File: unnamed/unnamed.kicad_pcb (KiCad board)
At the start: 2 copper layers, 33 parts, among them SW1 SW_Push, SW10 SW_Push, SW11 SW_Push, SW12 SW_Push, SW13 SW_Push, SW14 SW_Push, SW15 SW_Push, SW16 SW_Push, SW17 SW_Push, SW18 SW_Push, SW19 SW_Push, SW2 SW_Push, SW20 SW_Push, SW21 SW_Push, SW22 SW_Push, SW23 SW_Push, SW24 SW_Push, SW25 SW_SPST, SW26 SW_SPST, SW27 SW_Push, SW28 SW_Push, SW29 SW_Push, SW3 SW_Push, SW30 SW_Push, SW31 SW_Push, SW32 SW_Push, SW33 SW_Push, SW4 SW_Push, SW5 SW_Push, SW6 SW_Push, SW7 SW_Push, SW8 SW_Push, SW9 SW_Push

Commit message: place switches
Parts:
- moved SW17 212.8 mm to (201.4, 106.7), turned to -30 degrees
- moved SW16 175.6 mm to (181.7, 98.4), turned to -15 degrees
- moved SW1 116.6 mm to (115.4, 51.2)
- moved SW2 115.9 mm to (115.4, 70.2)
- moved SW9 115.8 mm to (153.4, 71.1)
- moved SW3 115.8 mm to (115.4, 89.2)
- moved SW8 115.7 mm to (153.4, 52.1)
- moved SW13 115.5 mm to (191.4, 40.2)
- moved SW12 115.5 mm to (172.4, 75.7)
- moved SW4 115.5 mm to (134.4, 39.2)
- moved SW7 115.5 mm to (153.4, 33.1)
- moved SW6 115.5 mm to (134.4, 77.2)
- moved SW11 115.5 mm to (172.4, 56.6)
- moved SW10 115.5 mm to (172.4, 37.6)
- moved SW15 115.4 mm to (191.4, 78.2)
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
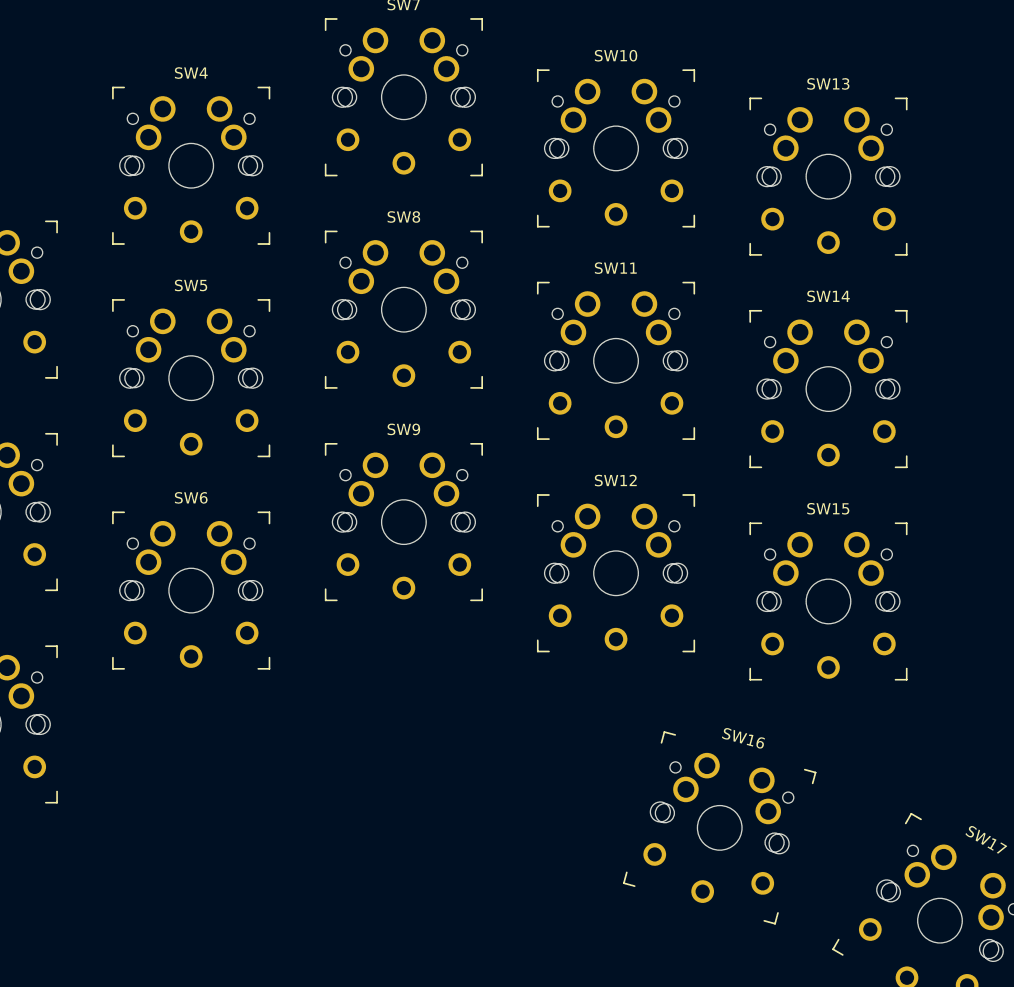
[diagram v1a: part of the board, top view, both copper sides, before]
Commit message: component placement
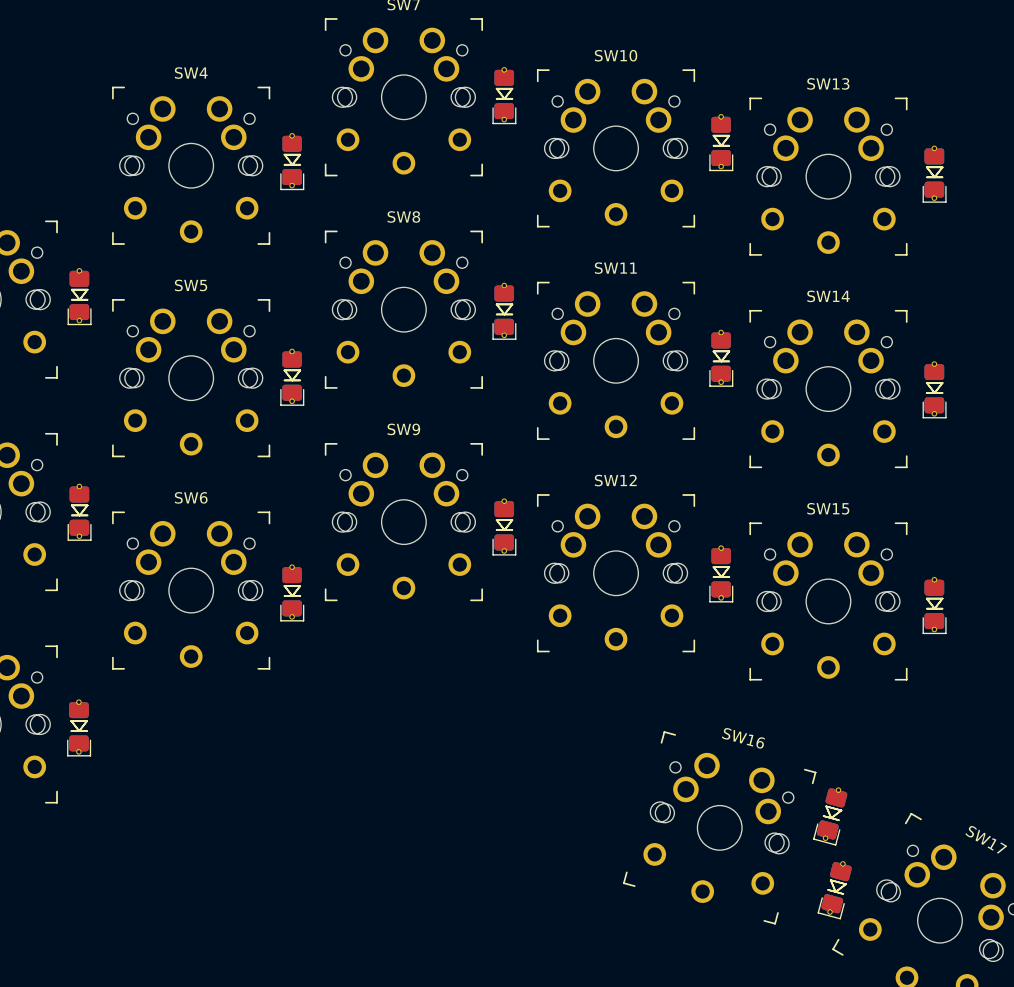
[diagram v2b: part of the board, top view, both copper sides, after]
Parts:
- added D10: D, Library:D_1206_handsolder_reversible, F.Cu at (143.4, 77.3)
- added D13: D, Library:D_1206_handsolder_reversible, F.Cu at (162.4, 32.8)
- added D14: D, Library:D_1206_handsolder_reversible, F.Cu at (162.4, 52.1)
- added D15: D, Library:D_1206_handsolder_reversible, F.Cu at (162.4, 71.4)
- added D18: D, Library:D_1206_handsolder_reversible, F.Cu at (181.8, 37.0)
- added D19: D, Library:D_1206_handsolder_reversible, F.Cu at (181.8, 56.3)
- added D20: D, Library:D_1206_handsolder_reversible, F.Cu at (181.8, 75.6)
- added D24: D, Library:D_1206_handsolder_reversible, F.Cu at (200.9, 39.9)
- added D25: D, Library:D_1206_handsolder_reversible, F.Cu at (200.9, 59.1)
- added D26: D, Library:D_1206_handsolder_reversible, F.Cu at (200.9, 78.4)
- added D3: D, Library:D_1206_handsolder_reversible, F.Cu at (124.4, 50.8)
- added D30: D, Library:D_1206_handsolder_reversible, F.Cu at (191.8, 97.2)
- added D33: D, Library:D_1206_handsolder_reversible, F.Cu at (192.2, 103.8)
- added D4: D, Library:D_1206_handsolder_reversible, F.Cu at (124.4, 70.1)
- added D5: D, Library:D_1206_handsolder_reversible, F.Cu at (124.4, 89.4)
- added D8: D, Library:D_1206_handsolder_reversible, F.Cu at (143.4, 38.7)
- added D9: D, Library:D_1206_handsolder_reversible, F.Cu at (143.4, 58.0)

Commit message: routing
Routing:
- net row3_l: track 0.00 -> 194.1 mm
- net row2_l: track 0.00 -> 178.4 mm
- net row4_l: track 0.00 -> 177.8 mm
- net col2_l: track 0.00 -> 128.1 mm, vias 0 -> 1
- net col3_l: track 0.00 -> 106.4 mm, vias 0 -> 1
- net col4_l: track 0.00 -> 85.1 mm, vias 0 -> 1
- net col5_l: track 0.00 -> 69.3 mm, vias 0 -> 1
- net col6_l: track 0.00 -> 50.2 mm, vias 0 -> 1
- net Net-(D26-Pad2): track 0.00 -> 25.9 mm
- net Net-(D25-Pad2): track 0.00 -> 25.7 mm
- net Net-(D20-Pad2): track 0.00 -> 25.7 mm
- net Net-(D18-Pad2): track 0.00 -> 25.7 mm
- net Net-(D24-Pad2): track 0.00 -> 25.6 mm
- net Net-(D19-Pad2): track 0.00 -> 25.5 mm
- net Net-(D8-Pad2): track 0.00 -> 25.4 mm
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
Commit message: drc
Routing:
- net col2_l: track 128.1 -> 123.2 mm
- net col3_l: track 106.4 -> 102.7 mm
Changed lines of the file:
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@@
   (segment (start 126.325 89.689264) (end 126.325 70.375) (width 0.2) (layer "F.Cu") (net 43))
   (segment (start 126.325 70.440882) (end 126.325 70.375) (width 0.2) (layer "F.Cu") (net 43))
-  (segment (start 126.325 69.1) (end 126.325 51.15) (width 0.2) (layer "F.Cu") (net 43))
-  (segment (start 124.425 53.05) (end 126.325 51.15) (width 0.2) (layer "F.Cu") (net 43))
+  (segment (start 126.325 54.95) (end 126.325 55.2) (width 0.2) (layer "F.Cu") (net 43))
+  (segment (start 124.425 53.05) (end 126.325 54.95) (width 0.2) (layer "F.Cu") (net 43))
   (segment (start 126.325 70.375) (end 126.325 69.1) (width 0.2) (layer "F.Cu") (net 43))
-  (segment (start 126.325 51.15) (end 126.325 50.05) (width 0.2) (layer "F.Cu") (net 43))
   (segment (start 124.3825 91.631764) (end 126.325 89.689264) (width 0.2) (layer "F.Cu") (net 43))
+  (segment (start 126.325 69.1) (end 126.325 55.2) (width 0.2) (layer "F.Cu") (net 43))
   (via (at 126.325 69.1) (size 0.5) (drill 0.3) (layers "F.Cu" "B.Cu") (net 43))
   (segment (start 158.535663 63.77248) (end 161.906591 67.143409) (width 0.2) (layer "B.Cu") (net 43))
@@
   (segment (start 146.82752 63.77248) (end 158.535663 63.77248) (width 0.2) (layer "B.Cu") (net 43))
   (segment (start 143.45 60.265882) (end 145.15 58.565882) (width 0.2) (layer "F.Cu") (net 44))
-  (segment (start 144.4625 40.2125) (end 145.15 39.525) (width 0.2) (layer "F.Cu") (net 44))
-  (segment (start 143.45 40.2125) (end 144.4625 40.2125) (width 0.2) (layer "F.Cu") (net 44))
   (segment (start 145.15 66.525) (end 145.15 58.565882) (width 0.2) (layer "F.Cu") (net 44))
-  (segment (start 145.15 39.525) (end 145.15 38.5) (width 0.2) (layer "F.Cu") (net 44))
+  (segment (start 145.15 58.565882) (end 145.15 42.625) (width 0.2) (layer "F.Cu") (net 44))
+  (segment (start 143.45 40.975) (end 145.1 42.625) (width 0.2) (layer "F.Cu") (net 44))
+  (segment (start 145.1 42.625) (end 145.15 42.625) (width 0.2) (layer "F.Cu") (net 44))
   (segment (start 143.45 79.556764) (end 145.15 77.856764) (width 0.2) (layer "F.Cu") (net 44))
-  (segment (start 145.15 58.565882) (end 145.15 39.525) (width 0.2) (layer "F.Cu") (net 44))
   (segment (start 145.15 77.856764) (end 145.15 66.525) (width 0.2) (layer "F.Cu") (net 44))
   (via (at 145.15 66.525) (size 0.5) (drill 0.3) (layers "F.Cu" "B.Cu") (net 44))

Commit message: routing
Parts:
- added FB1: FerriteBead, BK-CirqueDB:L_0805_2012Metric_Pad1.15x1.40mm_HandSolder, F.Cu at (304.8, 28.2)
- added FB2: FerriteBead, BK-CirqueDB:L_0805_2012Metric_Pad1.15x1.40mm_HandSolder, F.Cu at (275.2, 28.0)
- added FB3: FerriteBead, BK-CirqueDB:L_0805_2012Metric_Pad1.15x1.40mm_HandSolder, F.Cu at (275.1, 48.2)
- added FB4: FerriteBead, BK-CirqueDB:L_0805_2012Metric_Pad1.15x1.40mm_HandSolder, F.Cu at (306.1, 48.4)
- added H1: MountingHole_Pad, BK-CirqueDB:MountingHole_2.2mm_M2_Pad, F.Cu at (304.8, 23.5)
- added H2: MountingHole_Pad, BK-CirqueDB:MountingHole_2.2mm_M2_Pad, F.Cu at (276.8, 23.5)
- added H3: MountingHole_Pad, BK-CirqueDB:MountingHole_2.2mm_M2_Pad, F.Cu at (275.2, 53.0)
- added H4: MountingHole_Pad, BK-CirqueDB:MountingHole_2.2mm_M2_Pad, F.Cu at (306.2, 53.0)
- added J1: Conn_01x12_Female, BK-CirqueDB:CirqueDB-BK, F.Cu at (306.8, 61.3)
- added J5: S3B-PH-SM4-TB(LF)(SN), Connector_JST:JST_PH_S3B-PH-SM4-TB_1x03-1MP_P2.00mm_Horizontal, F.Cu at (383.6, 22.3)
- added J6: S3B-PH-SM4-TB(LF)(SN), Connector_JST:JST_PH_S3B-PH-SM4-TB_1x03-1MP_P2.00mm_Horizontal, F.Cu at (344.2, 44.9)
- added O3: trackpad, Connector_PinHeader_2.54mm:PinHeader_1x04_P2.54mm_Vertical, F.Cu at (219.7, 91.4)
- added U2: eliteC, Library:Elite-C, F.Cu at (223.6, 51.0)
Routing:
- net (no net): track 0.00 -> 278.9 mm
- net row1_l: track 5.92 -> 130.2 mm
- net col4_l: track 85.1 -> 161.7 mm, vias 1 -> 2
- net unconnected-(U2-Pad27): track 0.00 -> 74.2 mm
- net col2_l: track 123.2 -> 185.5 mm, vias 1 -> 2
- net unconnected-(U2-Pad26): track 0.00 -> 46.1 mm, vias 0 -> 1
- net col6_l: track 50.2 -> 95.7 mm
- net row4_l: track 177.8 -> 222.7 mm
- net mosi_l: track 0.00 -> 35.6 mm
- net Net-(D33-Pad2): track 2.91 -> 37.8 mm
- net Net-(D30-Pad2): track 3.02 -> 28.4 mm
- net col5_l: track 69.3 -> 90.6 mm
- net row3_l: track 194.1 -> 212.1 mm
- net row2_l: track 178.4 -> 194.3 mm
- net col3_l: track 102.7 -> 117.1 mm
- added copper zone on B.Cu, net (none)
- added copper zone on F.Cu, net (none)
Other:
- board outline added: 37 x 45.1 mm
- board text added: "SCL"
- board text added: "SDA"
- board text added: "VCC"

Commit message: routing
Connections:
- U2 pad 20: unconnected-(U2-Pad20) -> hand
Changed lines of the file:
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@@
   (net 62 "ss_l")
   (net 63 "+3V3")
-  (net 64 "unconnected-(U2-Pad20)")
-  (net 65 "unconnected-(U2-Pad29)")
+  (net 64 "unconnected-(U2-Pad29)")
+  (net 65 "hand")
   (footprint "Library:D_1206_handsolder_reversible" (layer "F.Cu")
     (at 200.9 39.85 90)
@@
       (net 19 "row1_l") (pinfunction "F5") (pintype "bidirectional"))
     (pad "20" thru_hole circle (at -3.81 -7.62 270) (size 1.7526 1.7526) (drill 1.0922) (layers *.Cu *.SilkS *.Mask)
-      (net 64 "unconnected-(U2-Pad20)") (pinfunction "F4") (pintype "bidirectional"))
+      (net 65 "hand") (pinfunction "F4") (pintype "bidirectional"))
     (pad "21" thru_hole circle (at -6.35 -7.62 270) (size 1.7526 1.7526) (drill 1.0922) (layers *.Cu *.SilkS *.Mask)
       (net 57 "Vcc_l") (pinfunction "VCC") (pintype "power_in"))
@@
       (net 61 "unconnected-(U2-Pad28)") (pinfunction "F1") (pintype "bidirectional+no_connect"))
     (pad "29" thru_hole circle (at 13.97 -5.08 270) (size 1.7526 1.7526) (drill 1.0922) (layers *.Cu *.SilkS *.Mask)
-      (net 65 "unconnected-(U2-Pad29)") (pinfunction "F0") (pintype "bidirectional+no_connect"))
+      (net 64 "unconnected-(U2-Pad29)") (pinfunction "F0") (pintype "bidirectional+no_connect"))
     (model "/Users/danny/Documents/proj/custom-keyboard/kicad-libs/3d_models/ArduinoProMicro.wrl"
       (offset (xyz -13.96999979 -7.619999886 -5.841999912))

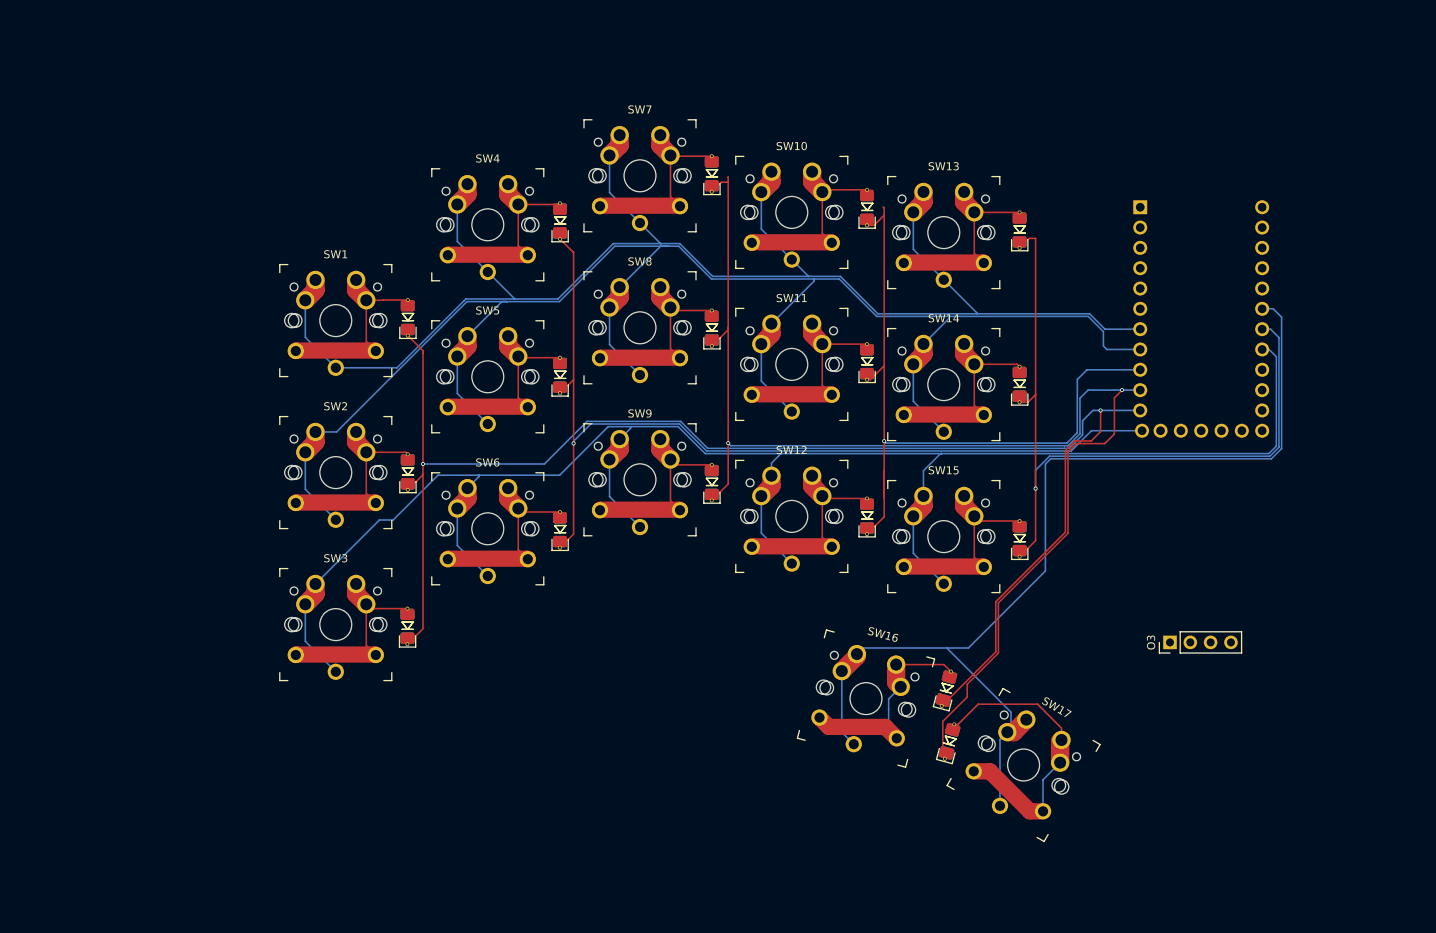
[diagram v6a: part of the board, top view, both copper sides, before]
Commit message: trackpad connector
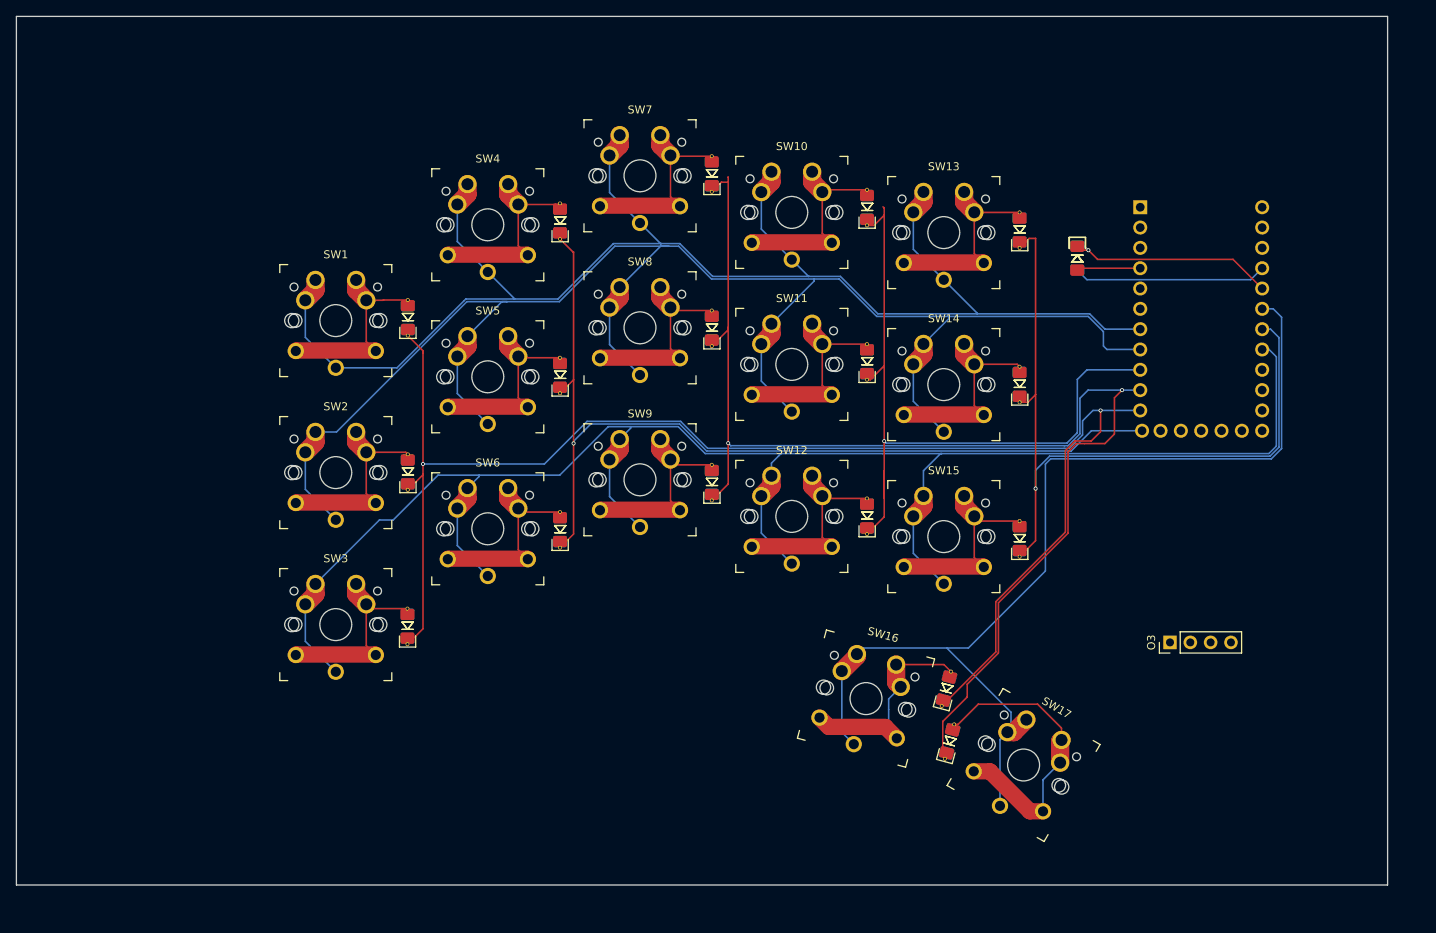
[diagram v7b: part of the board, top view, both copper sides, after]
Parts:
- added R7: 5.1k, footprints:D_1206_handsolder, B.Cu at (208.1, 43.4)
- added R8: 5.1k, footprints:D_1206_handsolder, F.Cu at (208.1, 43.4)
- J1: value Conn_01x12_Female -> Serial
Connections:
- O3 pad 1: +3V3 -> Vcc_l
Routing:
- net hand: track 0.00 -> 26.9 mm, vias 0 -> 1
- net Vcc_l: track 0.00 -> 24.2 mm
- net Gnd_l: track 0.00 -> 7.97 mm
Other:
- board size 37 x 45.1 mm -> 171.4 x 108.6 mm

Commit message: cleanup (reversible)
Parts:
- removed J5, J6: S3B-PH-SM4-TB(LF)(SN), Connector_JST:JST_PH_S3B-PH-SM4-TB_1x03-1MP_P2.00mm_Horizontal
- removed SW18, SW19, SW20, SW21, SW22, SW23, SW24, SW27, SW28, SW29, SW30, SW31, SW32, SW33: SW_Push, Library:SW_MX_choc
- removed SW25, SW26: SW_SPST, Library:SW_MX_choc
- D10, D13, D14, D15, D18, D19, D20, D24, D25, D26, D3, D30, D33, D4, D5, D8, D9: footprint Library:D_1206_handsolder_reversible -> footprints:D_1206_handsolder_reversible
- O3: footprint Connector_PinHeader_2.54mm:PinHeader_1x04_P2.54mm_Vertical -> footprints:PinHeader_1x04_P2.54mm_Vertical
- SW1, SW10, SW11, SW12, SW13, SW14, SW15, SW16, SW17, SW2, SW3, SW4, SW5, SW6, SW7, SW8, SW9: footprint Library:SW_MX_choc -> footprints:SW_MX_choc
- U2: footprint Library:Elite-C -> footprints:Elite-C
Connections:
- D10 pad 1: col3_l -> col2_l
- D13 pad 1: col4_l -> col3_l
- D14 pad 1: col4_l -> col3_l
- D15 pad 1: col4_l -> col3_l
- D18 pad 1: col5_l -> col4_l
- D19 pad 1: col5_l -> col4_l
- D20 pad 1: col5_l -> col4_l
- D24 pad 1: col6_l -> col5_l
- D25 pad 1: col6_l -> col5_l
- D26 pad 1: col6_l -> col5_l
- D3 pad 1: col2_l -> col1_l
- D30 pad 1: col2_l -> col1_l
- D33 pad 1: col4_l -> col3_l
- D4 pad 1: col2_l -> col1_l
- D5 pad 1: col2_l -> col1_l
- D8 pad 1: col3_l -> col2_l
- D9 pad 1: col3_l -> col2_l
- U2 pad 10: col4_l -> col3_l
- U2 pad 11: col2_l -> col1_l
- U2 pad 12: col3_l -> col2_l
- U2 pad 18: col6_l -> col5_l
- U2 pad 9: col5_l -> col4_l
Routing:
- net col1_l: track 0.00 -> 185.5 mm, vias 0 -> 2
- net col6_l: track 95.7 -> 0.00 mm, vias 1 -> 0
- net col4_l: track 161.7 -> 90.6 mm, vias 2 -> 1
- net col2_l: track 185.5 -> 117.1 mm, vias 2 -> 1
- net col3_l: track 117.1 -> 161.7 mm, vias 1 -> 2
- net col5_l: track 90.6 -> 95.7 mm
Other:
- board text added: "BAT"
- board text added: "C1R2"
- board text added: "C1R3"
- board text added: "C1R4"
- board text added: "C2"
- board text added: "C2R1"
- board text added: "C2R2"
- board text added: "C2R3"
- board text added: "C2R4"
- board text added: "C3"
- board text added: "C3R2"
- board text added: "C3R3"
- board text added: "C3R4"
- board text added: "C4"
- board text added: "C4R1"
- board text added: "C4R2"
- board text added: "C4R3"
- board text added: "C4R4"
- board text added: "C5"
- board text added: "C5R2"
- board text added: "C5R3"
- board text added: "C5R4"
- board text added: "C6"
- board text added: "HAND"
- board text added: "MISO"
- board text added: "MOSI"
- board text added: "R1"
- board text added: "R2"
- board text added: "R3"
- board text added: "R4"
- board text added: "RGB"
- board text added: "RST"
- board text added: "SC"
- board text added: "SERIAL"
- board text added: "SS"
